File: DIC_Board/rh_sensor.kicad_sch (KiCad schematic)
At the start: 0 parts

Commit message: Wrapping up schematic
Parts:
- added J6: Conn_01x04, symbol Connector_Generic:Conn_01x04
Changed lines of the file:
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@@
 	(generator_version "10.0")
 	(paper "A4")
+	(symbol
+		(lib_id "Connector_Generic:Conn_01x04")
+		(at 218.44 86.36 0)
+		(unit 1)
+		(body_style 1)
+		(exclude_from_sim no)
+		(in_bom yes)
+		(on_board yes)
+		(in_pos_files yes)
+		(dnp no)
+		(fields_autoplaced yes)
+		(property "Reference" "J6"
+			(at 220.98 86.3599 0)
+			(show_name no)
+			(do_not_autoplace no)
+			(effects
+				(font
+					(size 1.27 1.27)
+				)
+				(justify left)
+			)
+		)
+		(property "Value" "Conn_01x04"
+			(at 220.98 88.8999 0)
+			(show_name no)
+			(do_not_autoplace no)
+			(effects
+				(font
+					(size 1.27 1.27)
+				)
+				(justify left)
+			)
+		)
+		(property "Footprint" ""
+			(at 218.44 86.36 0)
+			(hide yes)
+			(show_name no)
+			(do_not_autoplace no)
+			(effects
+				(font
+					(size 1.27 1.27)
+				)
+			)
+		)
+		(property "Datasheet" ""
+			(at 218.44 86.36 0)
+			(hide yes)
+			(show_name no)
+			(do_not_autoplace no)
+			(effects
+				(font
+					(size 1.27 1.27)
+				)
+			)
+		)
+		(property "Description" "Generic connector, single row, 01x04, script generated (kicad-library-utils/schlib/autogen/connector/)"
+			(at 218.44 86.36 0)
+			(hide yes)
+			(show_name no)
+			(do_not_autoplace no)
+			(effects
+				(font
+					(size 1.27 1.27)
+				)
+			)
+		)
+		(pin "1"
+		)
+		(pin "4"
+		)
+		(pin "3"
+		)
+		(pin "2"
+		)
+		(instances
+			(project "DIC_Board"
+				(path "/bb0ef0df-c181-443a-843c-695cd2e0efee/15388a04-aea8-414b-8903-58a719a8054d/a18bb969-316f-4822-a8ba-f772f1045bbc"
+					(reference "J6")
+					(unit 1)
+				)
+			)
+		)
+	)
 )

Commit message: Checkpoint current schematic state
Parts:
- added R343, R344: 4.7k, symbol Device:R
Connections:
- net GND: now reaches J6.1 (Pin_1)
- net RH_SDA: now reaches J6.2 (Pin_2)
- net RH_SDA: now also R343.1
- net RH_SCL: now reaches J6.3 (Pin_3)
- net RH_SCL: now also R344.1
- net +3V3: now reaches J6.4 (Pin_4)
- net +3V3: now also R343.2, R344.2
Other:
- moved on the sheet: J6

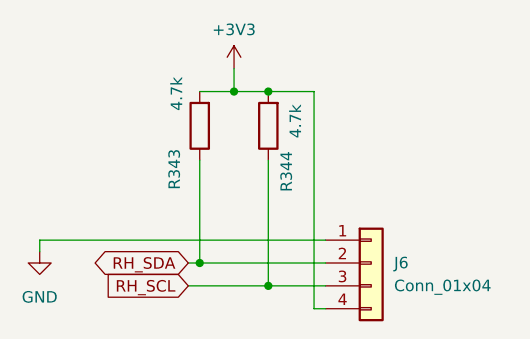
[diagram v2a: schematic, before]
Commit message: Synchronize schematic hierarchy and MCU pin map
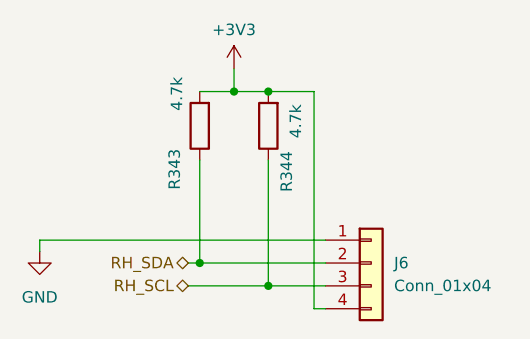
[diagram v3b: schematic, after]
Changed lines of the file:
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@@
 		)
 	)
-	(global_label "RH_SCL"
-		(shape input)
+	(hierarchical_label "RH_SCL"
+		(shape bidirectional)
 		(at 124.46 104.14 180)
-		(fields_autoplaced yes)
 		(effects
 			(font
@@
 			(justify right)
 		)
-		(property "Intersheetrefs" "${INTERSHEET_REFS}"
-			(at 114.3991 104.14 0)
-			(hide yes)
-			(show_name no)
-			(do_not_autoplace no)
-			(effects
-				(font
-					(size 1.27 1.27)
-				)
-				(justify right)
-			)
-		)
 	)
-	(global_label "RH_SDA"
+	(hierarchical_label "RH_SDA"
 		(shape bidirectional)
 		(at 124.46 101.6 180)
-		(fields_autoplaced yes)
 		(effects
 			(font
@@
 			(justify right)
 		)
-		(property "Intersheetrefs" "${INTERSHEET_REFS}"
-			(at 113.2273 101.6 0)
-			(hide yes)
-			(show_name no)
-			(do_not_autoplace no)
-			(effects
-				(font
-					(size 1.27 1.27)
-				)
-				(justify right)
-			)
-		)
 	)

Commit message: Updated board for layout! All footprints added
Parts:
- J6: footprint (none) -> Connector_Molex:Molex_Micro-Fit_3.0_43045-0400_2x02_P3.00mm_Horizontal; BOM Source (none) -> https://www.molex.com/en-us/products/part-detail/430450400; MPN (none) -> 0430450400; Manufacturer (none) -> Molex
- R343, R344: footprint (none) -> Resistor_SMD:R_0603_1608Metric; BOM Source (none) -> https://www.vishay.com/docs/20035/dcrcwe3.pdf; MPN (none) -> CRCW06034K70FKEA; Manufacturer (none) -> Vishay; Power Rating (none) -> 0.125W; Tolerance (none) -> 1%
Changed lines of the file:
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@@
 			)
 		)
-		(property "Footprint" ""
+		(property "Footprint" "Resistor_SMD:R_0603_1608Metric"
 			(at 133.35 86.36 0)
 			(hide yes)
@@
 			)
 		)
-		(property "MPN" ""
+		(property "MPN" "CRCW06034K70FKEA"
 			(at 133.35 86.36 0)
 			(hide yes)
@@
 			)
 		)
-		(property "Manufacturer" ""
+		(property "Manufacturer" "Vishay"
 			(at 133.35 86.36 0)
+			(hide yes)
+			(show_name no)
+			(do_not_autoplace no)
+			(effects
+				(font
+					(size 1.27 1.27)
+				)
+			)
+		)
+		(property "Tolerance" "1%"
+			(at 0 0 0)
+			(hide yes)
+			(show_name no)
+			(do_not_autoplace no)
+			(effects
+				(font
+					(size 1.27 1.27)
+				)
+			)
+		)
+		(property "Power Rating" "0.125W"
+			(at 0 0 0)
+			(hide yes)
+			(show_name no)
+			(do_not_autoplace no)
+			(effects
+				(font
+					(size 1.27 1.27)
+				)
+			)
+		)
+		(property "BOM Source" "https://www.vishay.com/docs/20035/dcrcwe3.pdf"
+			(at 0 0 0)
 			(hide yes)
 			(show_name no)
@@
 			)
 		)
-		(property "Footprint" ""
+		(property "Footprint" "Connector_Molex:Molex_Micro-Fit_3.0_43045-0400_2x02_P3.00mm_Horizontal"
 			(at 144.78 101.6 0)
 			(hide yes)
@@
 		(property "Description" "Generic connector, single row, 01x04, script generated (kicad-library-utils/schlib/autogen/connector/)"
 			(at 144.78 101.6 0)
+			(hide yes)
+			(show_name no)
+			(do_not_autoplace no)
+			(effects
+				(font
+					(size 1.27 1.27)
+				)
+			)
+		)
+		(property "MPN" "0430450400"
+			(at 0 0 0)
+			(hide yes)
+			(show_name no)
+			(do_not_autoplace no)
+			(effects
+				(font
+					(size 1.27 1.27)
+				)
+			)
+		)
+		(property "Manufacturer" "Molex"
+			(at 0 0 0)
+			(hide yes)
+			(show_name no)
+			(do_not_autoplace no)
+			(effects
+				(font
+					(size 1.27 1.27)
+				)
+			)
+		)
+		(property "BOM Source" "https://www.molex.com/en-us/products/part-detail/430450400"
+			(at 0 0 0)
 			(hide yes)
 			(show_name no)
@@
 			)
 		)
-		(property "Footprint" ""
+		(property "Footprint" "Resistor_SMD:R_0603_1608Metric"
 			(at 125.73 86.36 0)
 			(hide yes)
@@
 			)
 		)
-		(property "MPN" ""
+		(property "MPN" "CRCW06034K70FKEA"
 			(at 125.73 86.36 0)
 			(hide yes)
@@
 			)
 		)
-		(property "Manufacturer" ""
+		(property "Manufacturer" "Vishay"
 			(at 125.73 86.36 0)
 			(hide yes)
 			(show_name no)
+			(do_not_autoplace no)
+			(effects
+				(font
+					(size 1.27 1.27)
+				)
+			)
+		)
+		(property "Tolerance" "1%"
+			(at 0 0 0)
+			(hide yes)
+			(show_name no)
+			(do_not_autoplace no)
+			(effects
+				(font
+					(size 1.27 1.27)
+				)
+			)
+		)
+		(property "Power Rating" "0.125W"
+			(at 0 0 0)
+			(hide yes)
+			(show_name no)
+			(do_not_autoplace no)
+			(effects
+				(font
+					(size 1.27 1.27)
+				)
+			)
+		)
+		(property "BOM Source" "https://www.vishay.com/docs/20035/dcrcwe3.pdf"
+			(at 0 0 0)
+			(hide yes)
+			(show_name no)
